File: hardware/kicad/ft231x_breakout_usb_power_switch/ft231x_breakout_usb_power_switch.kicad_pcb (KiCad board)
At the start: 2 copper layers, 60 x 31.2 mm, 61 parts, among them J1 USB_B_Micro_ALT, J2 USB_A_ALT, J3 Conn_01x08, J4 Conn_01x06, J5 Conn_01x08, Q3 2N7002, SW1 B3U-1000P, U1 SRV05-4, U2 FT231XS, U3 TPS2553DBVR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

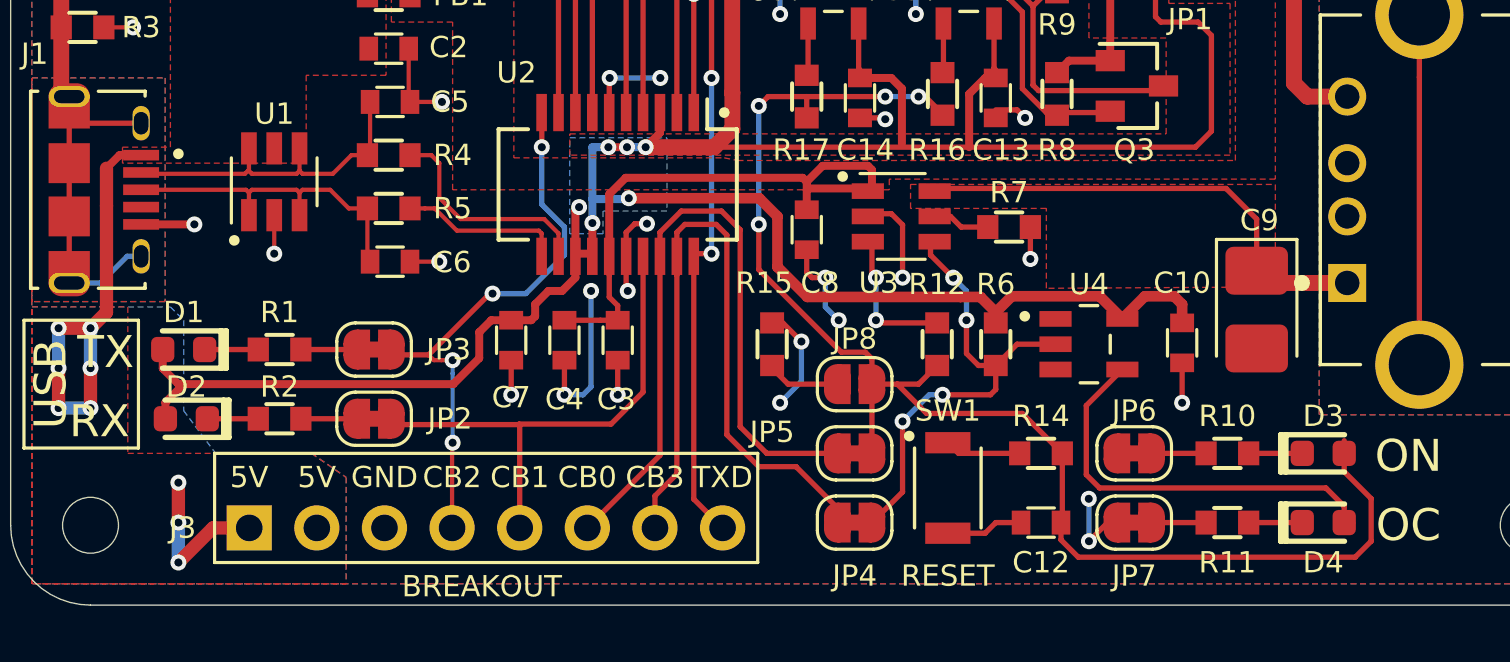
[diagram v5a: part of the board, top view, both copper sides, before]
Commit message: Fix reset when FT231X is drivng power switch OE
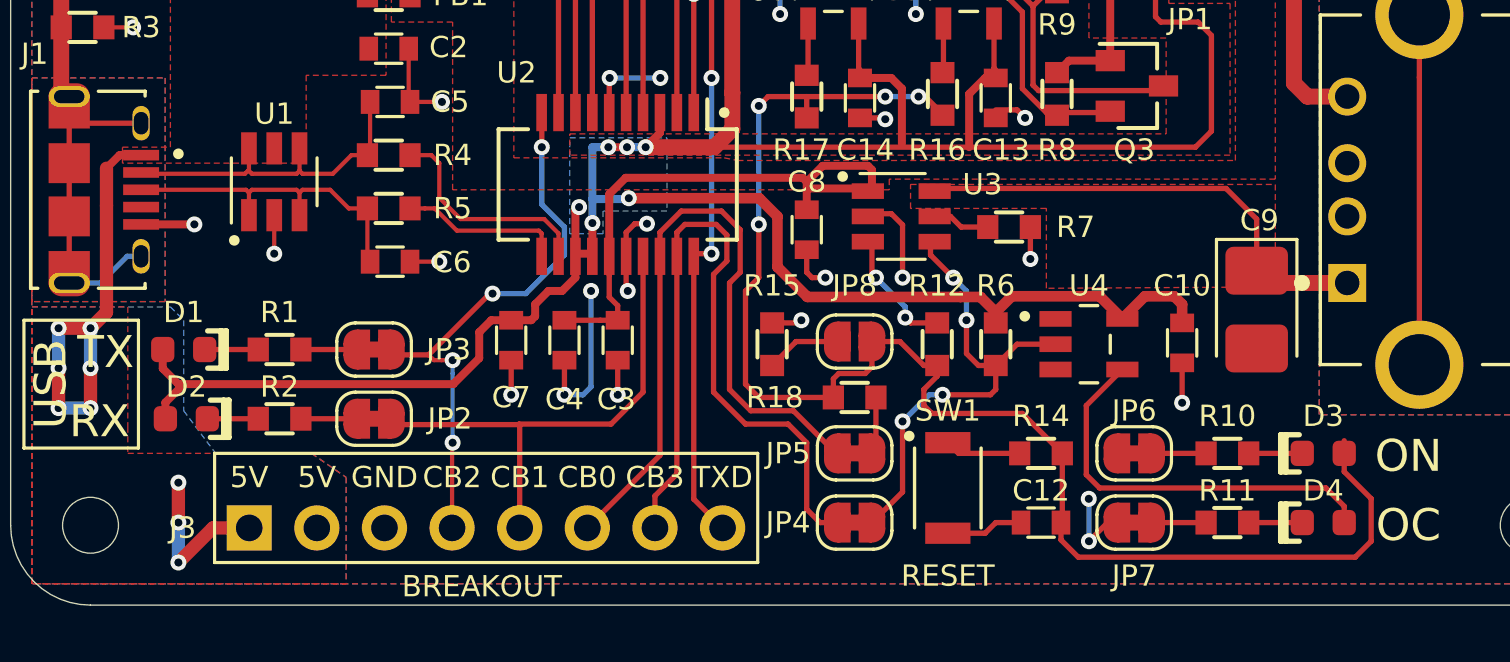
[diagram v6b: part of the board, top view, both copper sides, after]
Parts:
- added R18: 10k, -Passive:R_0603, F.Cu at (141.7, 92.8)
- moved JP8 1.60 mm to (141.7, 90.7)
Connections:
- JP5 pad 1: /EN -> Net-(JP5-Pad1)
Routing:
- net GND: track 69.1 -> 64.8 mm, vias 32 -> 30
- net /EN: track 53.1 -> 55.9 mm
- net Net-(JP5-Pad1): track 0.00 -> 2.16 mm
- net /GPI: track 26.9 -> 28.4 mm
- net Net-(R12-Pad2): track 5.93 -> 5.02 mm

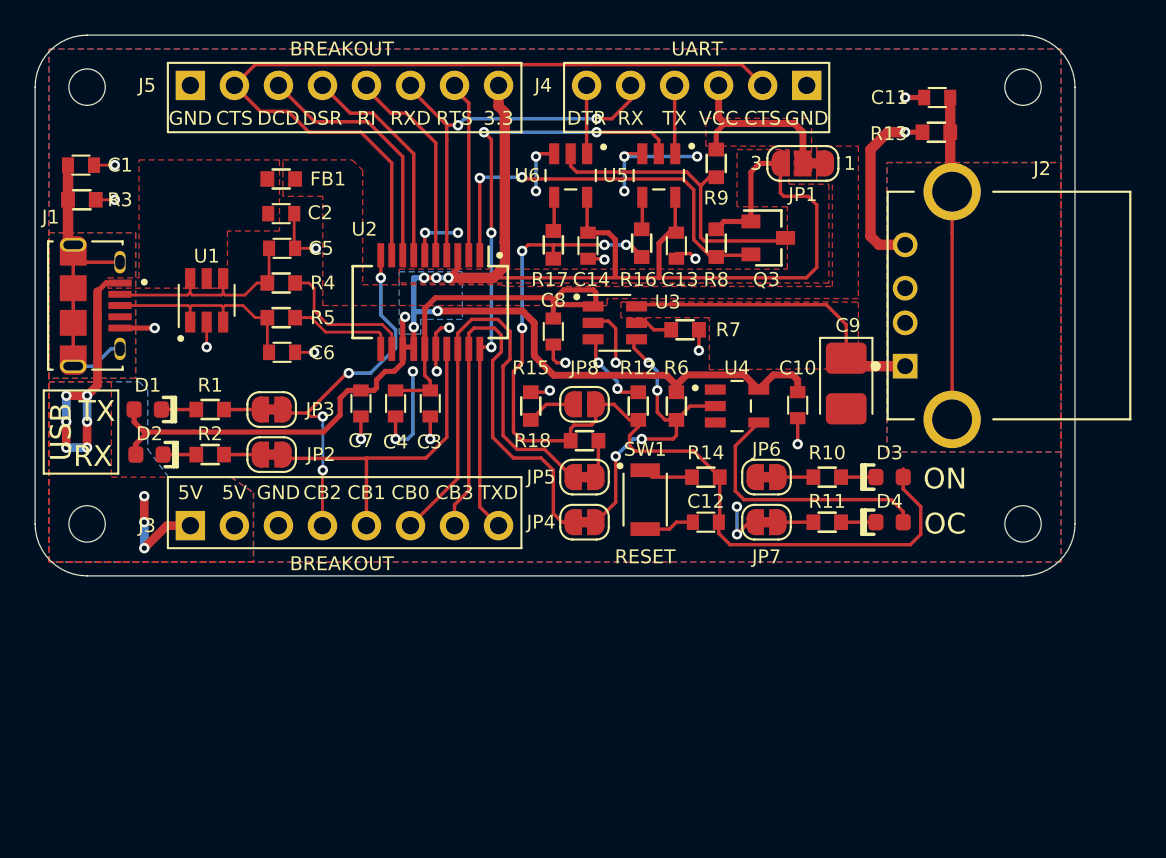
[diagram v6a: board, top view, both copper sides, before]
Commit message: KiBuzzard labels
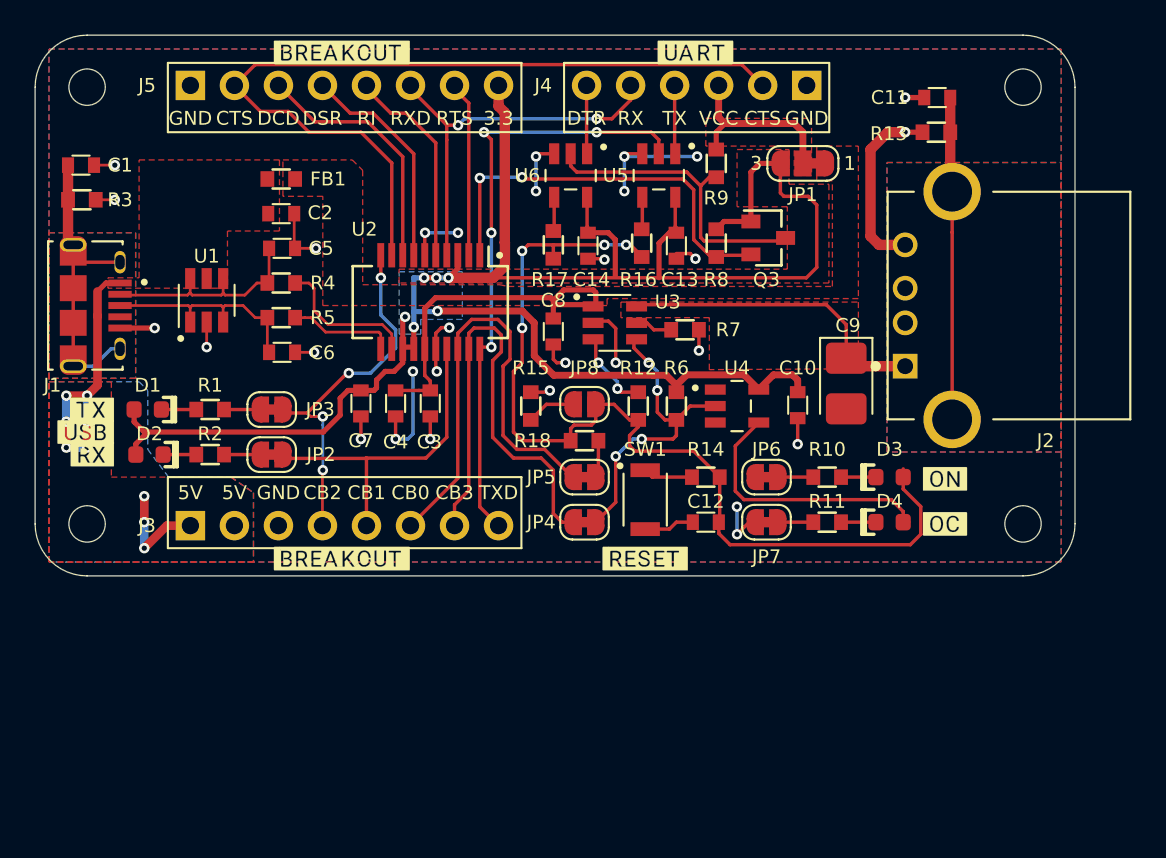
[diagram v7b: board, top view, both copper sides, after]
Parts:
- added ?: , buzzard_labels, F.Cu at (162.5, 97.6)
- added ?: , buzzard_labels, F.Cu at (162.5, 95.0)
- added ?: , buzzard_labels, F.Cu at (112.9, 92.3)
- added ?: , buzzard_labels, F.Cu at (113.3, 93.6)
- added ?: , buzzard_labels, F.Cu at (113.3, 91.0)
- added ?: , buzzard_labels, F.Cu at (145.2, 99.6)
- added ?: , buzzard_labels, F.Cu at (127.7, 99.6)
- added ?: , buzzard_labels, F.Cu at (127.7, 70.4)
- added ?: , buzzard_labels, F.Cu at (148.1, 70.4)
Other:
- board text added: "Short JP8 to default USB power to off."
- board text added: "VOUT UART is 5V, to change to 3.3V cut JP1 pads 1 & 2 and bridge JP1 pads 2 & 3."
- board text added: "ft231x_breakout_usb_power_switch"
- board text added: "v0.2"
- board text removed: "BREAKOUT"
- board text removed: "OC"
- board text removed: "ON"
- board text removed: "RESET"
- board text removed: "RX"
- board text removed: "TX"
- board text removed: "UART"
- board text removed: "USB"
- board text removed: "USB Power Switcher & UART"

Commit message: use github workflow to add hash to silkscreen
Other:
- board text added: "v0.2<<hash>>"
- board text removed: "v0.2"
